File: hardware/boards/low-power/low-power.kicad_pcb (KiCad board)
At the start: 4 copper layers, 128.5 x 45 mm, 202 parts, among them J101 Conn_01x05_Pin, J102 Conn_02x18_Top_Bottom, J103 Conn_01x04, J201 U.FL, J301 U.FL, J401 U.FL, J601 USB_C_Receptacle_USB2.0, Q201 DMP3013SFV, Q202 DMP3013SFV, Q801 DMN2400UFB4, SW501 SW_Push, SW601 SW_Push, U1002 TCA9539RTWR, U201 SW-GPS01, U202 LM75BTP,147, U203 BQ51013B, U301 TX5813, U401 SX1262IMLTRT, U402 SKY13453-385LF, U501 W25Q16JVUXIQ, U502 RP2040, U601 TCA9539RTWR, U602 TMUX1309BQBR, U603 CYPD3177, U701 LSM6DSM, U801 IS31FL3197, U901 AP63356QZV-7, U902 AP63356QZV-7, U903 INA2180A3IDSGR, Y401 32 MHz, Y501 12 MHz

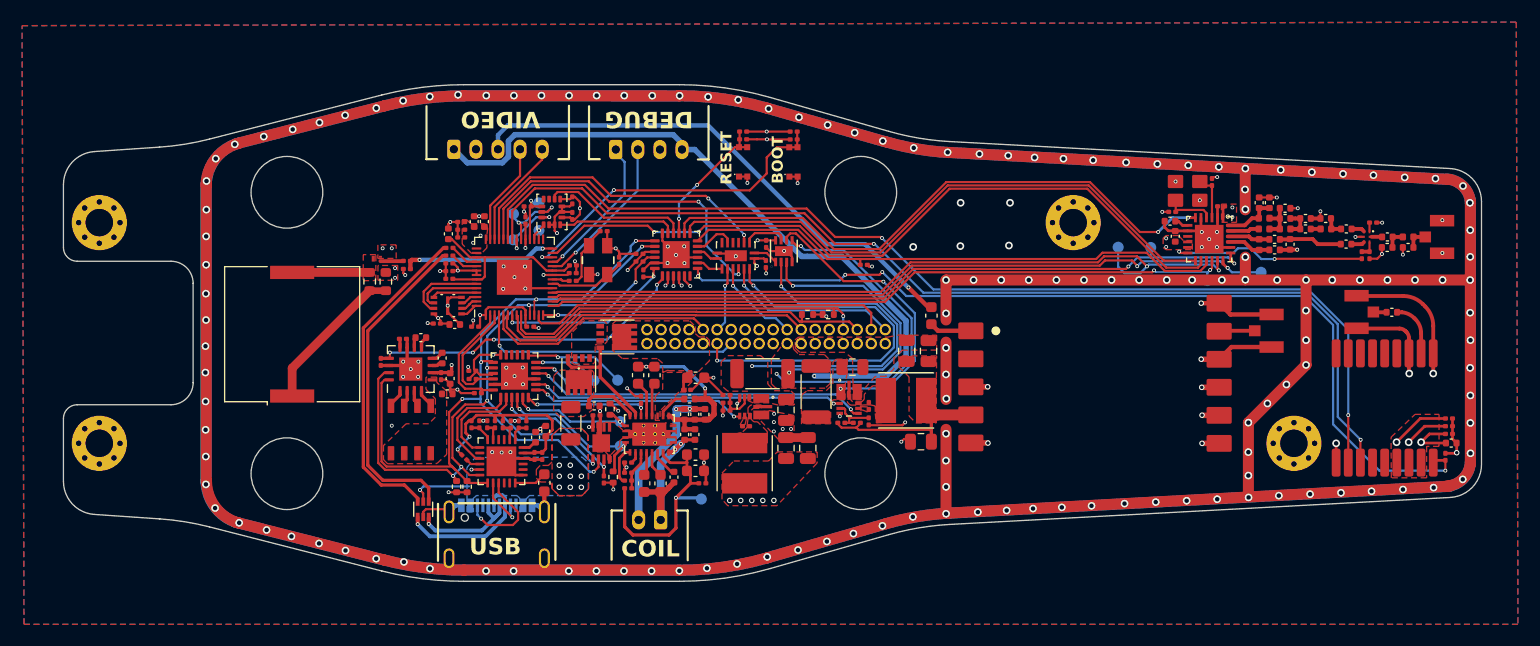
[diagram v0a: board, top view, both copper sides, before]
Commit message: fixup! Add low power PCB
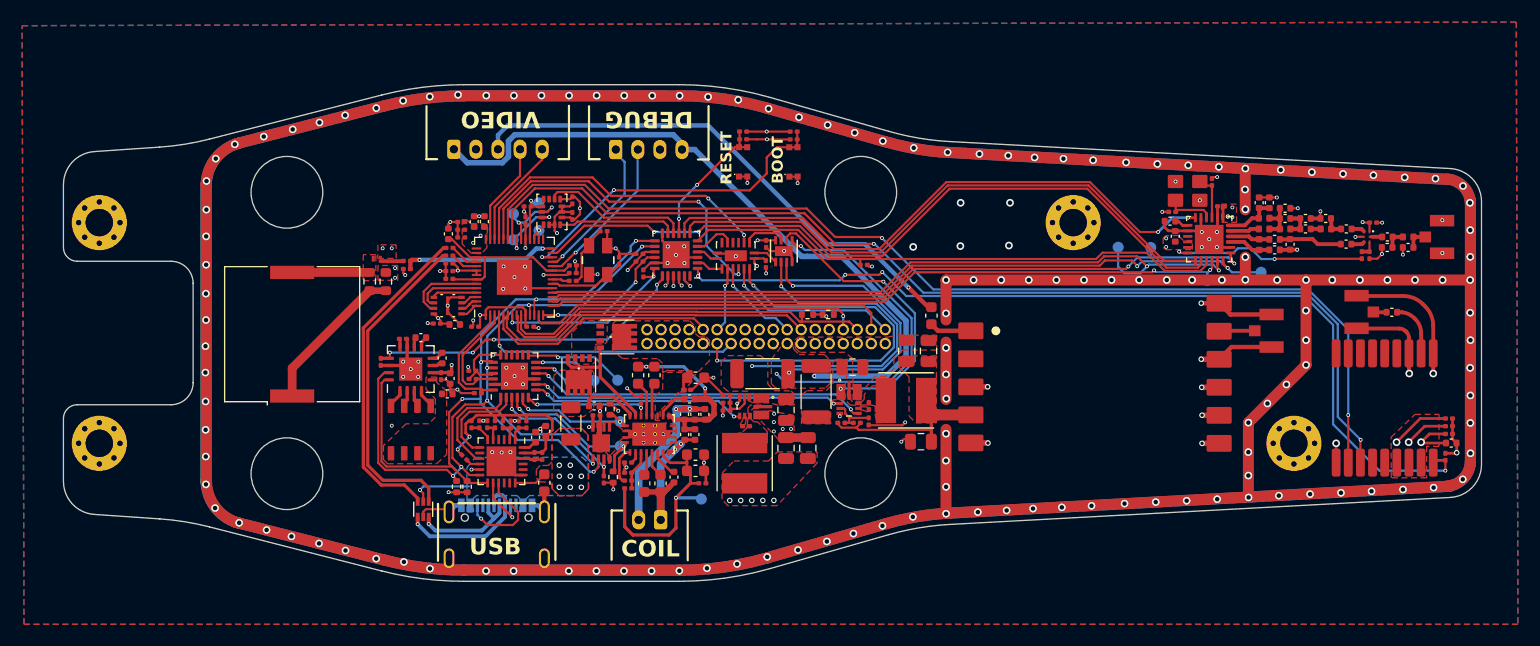
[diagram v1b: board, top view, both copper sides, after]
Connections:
- C419 pad 1: Net-(U402-VDD) -> +3V3
- U402 pad 1: Net-(U402-VDD) -> +3V3
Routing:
- net +3V3: track 66.8 -> 68.3 mm, vias 35 -> 36
- net Net-(U402-VDD): track 0.80 -> 0.00 mm
